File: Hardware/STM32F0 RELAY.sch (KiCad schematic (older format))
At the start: 28 parts, among them Q2 BSS138, U9 STM32F091RCT7, Y4 32.768kHz, Y5 8MHz

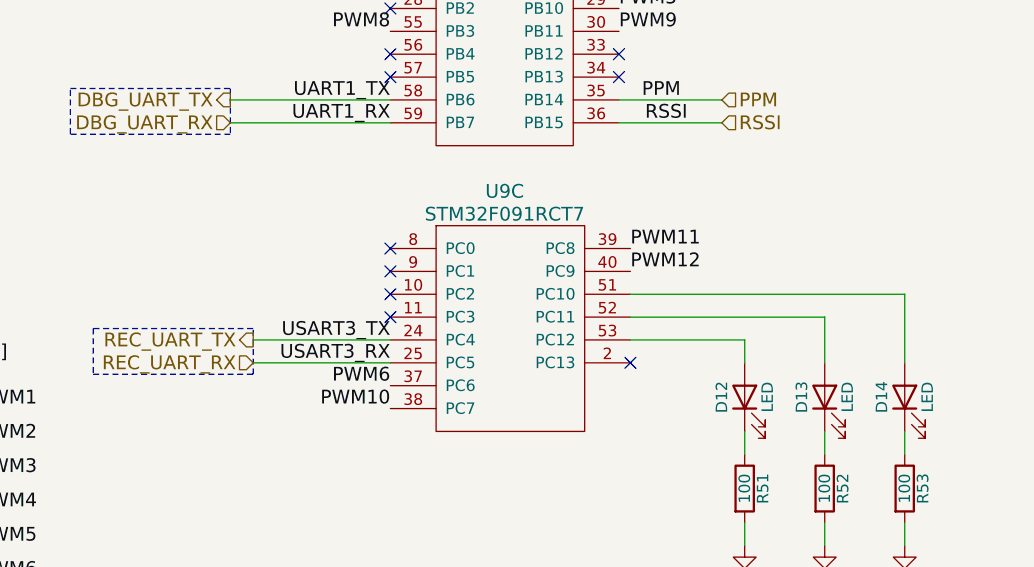
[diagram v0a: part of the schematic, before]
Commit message: Added additional headers to some interfaces, GPIOs, and FTDI pins. Added silks
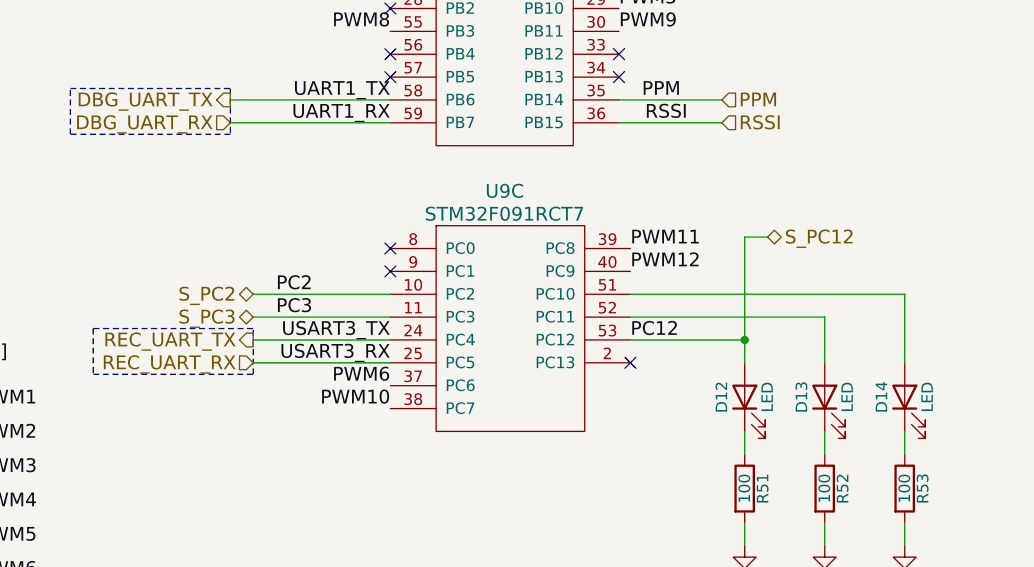
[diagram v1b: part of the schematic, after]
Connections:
- net S_PC12: now reaches D12.2 (A), U9.53 (PC12)
- net S_PC2: now reaches U9.10 (PC2)
- net S_PC3: now reaches U9.11 (PC3)
- no-connect marks 17 -> 15
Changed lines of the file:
@@
 $Descr A4 11693 8268
 encoding utf-8
-Sheet 9 10
+Sheet 8 10
 Title "Safety Switch Controller/ PPM Converter"
 Date "2017-05-14"
@@
 Wire Wire Line
 	7150 3150 7400 3150
-NoConn ~ 3900 5400
-NoConn ~ 3900 5300
 NoConn ~ 3900 5200
 NoConn ~ 3900 5100
@@
 Wire Wire Line
 	1400 2750 1400 2800
+Wire Wire Line
+	3900 5400 3300 5400
+Wire Wire Line
+	3900 5300 3300 5300
+Wire Wire Line
+	5450 5500 5450 5050
+Connection ~ 5450 5500
+Text Label 4950 5500 0    60   ~ 0
+PC12
+Text HLabel 3300 5300 0    60   BiDi ~ 0
+S_PC2
+Text HLabel 3300 5400 0    60   BiDi ~ 0
+S_PC3
+Text HLabel 5550 5050 2    60   BiDi ~ 0
+S_PC12
+Wire Wire Line
+	5450 5050 5550 5050
 Wire Bus Line
 	1850 5700 1850 7350
+Text Label 3400 5300 0    60   ~ 0
+PC2
+Text Label 3400 5400 0    60   ~ 0
+PC3
 $EndSCHEMATC

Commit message: associated components to their JLC part numbers
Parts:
- C65, C66: LCSC (none) -> C1644
- C67, C68: LCSC (none) -> C1679
- C69: LCSC (none) -> C57112
- C70: LCSC (none) -> C15849
- C71, C73, C74, C75: LCSC (none) -> C14663
- C72: LCSC (none) -> C19666
- D12, D13, D14: LCSC (none) -> C72043
- R5, R51, R52, R53, R6: LCSC (none) -> C22775
- R50: LCSC (none) -> C25803
- R54: LCSC (none) -> C25804
- U9: symbol WARG:STM32F091RCT7 -> ZP-Breakout-rescue:STM32F091RCT7-WARG; LCSC (none) -> C81046
- U9: symbol WARG:STM32F091RCT7 -> ZP-Breakout-rescue:STM32F091RCT7-WARG
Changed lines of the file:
@@
 EESchema Schematic File Version 4
-LIBS:ZP-Breakout-cache
-EELAYER 29 0
+EELAYER 30 0
 EELAYER END
 $Descr A4 11693 8268
@@
 F 3 "https://katalog.we-online.de/pbs/datasheet/885012006031.pdf" H 6550 2700 50  0001 C CNN
 F 4 "CAPP-009" H 6550 2700 60  0001 C CNN "part_num"
+F 5 "C1679" H 6550 2700 50  0001 C CNN "LCSC"
 	1    6550 2700
 	0    -1   -1   0
@@
 F 3 "https://katalog.we-online.de/pbs/datasheet/885012006031.pdf" H 6550 3000 50  0001 C CNN
 F 4 "CAPP-009" H 6550 3000 60  0001 C CNN "part_num"
+F 5 "C1679" H 6550 3000 50  0001 C CNN "LCSC"
 	1    6550 3000
 	0    -1   -1   0
@@
 F 3 "https://katalog.we-online.de/pbs/datasheet/885012006033.pdf" H 6550 2450 50  0001 C CNN
 F 4 "CAPP-008" H 6550 2450 60  0001 C CNN "part_num"
+F 5 "C1644" H 6550 2450 50  0001 C CNN "LCSC"
 	1    6550 2450
 	0    -1   -1   0
@@
 F 3 "https://katalog.we-online.de/pbs/datasheet/885012006033.pdf" H 6550 2150 50  0001 C CNN
 F 4 "CAPP-008" H 6550 2150 60  0001 C CNN "part_num"
+F 5 "C1644" H 6550 2150 50  0001 C CNN "LCSC"
 	1    6550 2150
 	0    -1   -1   0
@@
 F 3 "http://optoelectronics.liteon.com/upload/download/DS22-2000-228/LTST-C191KGKT.PDF" H 5800 5750 50  0001 C CNN
 F 4 "DIOD-002" H 5800 5750 60  0001 C CNN "part_num"
+F 5 "C72043" H 5800 5750 50  0001 C CNN "LCSC"
 	1    5800 5750
 	0    -1   -1   0
@@
 F 3 "http://www.yageo.com/documents/recent/PYu-RC_Group_51_RoHS_L_10.pdf" H 5800 6150 50  0001 C CNN
 F 4 "RESS-006" V 5800 6150 60  0001 C CNN "part_num"
+F 5 "C22775" V 5800 6150 50  0001 C CNN "LCSC"
 	1    5800 6150
 	1    0    0    -1
@@
 F 3 "http://optoelectronics.liteon.com/upload/download/DS22-2000-228/LTST-C191KGKT.PDF" H 5450 5750 50  0001 C CNN
 F 4 "DIOD-002" H 5450 5750 60  0001 C CNN "part_num"
+F 5 "C72043" H 5450 5750 50  0001 C CNN "LCSC"
 	1    5450 5750
 	0    -1   -1   0
@@
 F 3 "http://www.yageo.com/documents/recent/PYu-RC_Group_51_RoHS_L_10.pdf" H 5450 6150 50  0001 C CNN
 F 4 "RESS-006" V 5450 6150 60  0001 C CNN "part_num"
+F 5 "C22775" V 5450 6150 50  0001 C CNN "LCSC"
 	1    5450 6150
 	1    0    0    -1
@@
 F 3 "http://optoelectronics.liteon.com/upload/download/DS22-2000-228/LTST-C191KGKT.PDF" H 6150 5750 50  0001 C CNN
 F 4 "DIOD-002" H 6150 5750 60  0001 C CNN "part_num"
+F 5 "C72043" H 6150 5750 50  0001 C CNN "LCSC"
 	1    6150 5750
 	0    -1   -1   0
@@
 F 3 "http://www.yageo.com/documents/recent/PYu-RC_Group_51_RoHS_L_10.pdf" H 6150 6150 50  0001 C CNN
 F 4 "RESS-006" V 6150 6150 60  0001 C CNN "part_num"
+F 5 "C22775" V 6150 6150 50  0001 C CNN "LCSC"
 	1    6150 6150
 	1    0    0    -1
@@
 $EndComp
 $Comp
-L WARG:STM32F091RCT7 U9
+L ZP-Breakout-rescue:STM32F091RCT7-WARG U9
 U 5 1 599C1AE4
 P 8350 4900
@@
 F 3 "http://www.yageo.com/documents/recent/PYu-RC_Group_51_RoHS_L_10.pdf" H 7400 3300 50  0001 C CNN
 F 4 "RESS-005" V 7400 3300 60  0001 C CNN "part_num"
+F 5 " C25804" V 7400 3300 50  0001 C CNN "LCSC"
 	1    7400 3300
 	1    0    0    -1
@@
 F 3 "http://www.yageo.com/documents/recent/PYu-RC_Group_51_RoHS_L_10.pdf" H 2100 4350 50  0001 C CNN
 F 4 "RESS-008" V 2100 4350 60  0001 C CNN "part_num"
+F 5 "C25803" V 2100 4350 50  0001 C CNN "LCSC"
 	1    2100 4350
 	-1   0    0    -1
@@
 F 3 "https://search.murata.co.jp/Ceramy/image/img/A01X/G101/ENG/GRM188R71E104KA01-01.pdf" H 8400 5050 50  0001 C CNN
 F 4 "CAPP-005" H 8400 5050 60  0001 C CNN "part_num"
+F 5 "C14663" H 8400 5050 50  0001 C CNN "LCSC"
 	1    8400 5050
 	1    0    0    -1
@@
 F 3 "https://search.murata.co.jp/Ceramy/image/img/A01X/G101/ENG/GRM188R71H103KA01-01.pdf" H 6900 5050 50  0001 C CNN
 F 4 "CAPP-010" H 6900 5050 60  0001 C CNN "part_num"
+F 5 "C57112" H 6900 5050 50  0001 C CNN "LCSC"
 	1    6900 5050
 	1    0    0    -1
@@
 F 3 "https://search.murata.co.jp/Ceramy/image/img/A01X/G101/ENG/GRM188R61E105KA12-01.pdf" H 7150 5050 50  0001 C CNN
 F 4 "CAPP-004" H 7150 5050 60  0001 C CNN "part_num"
+F 5 "C15849" H 7150 5050 50  0001 C CNN "LCSC"
 	1    7150 5050
 	1    0    0    -1
@@
 F 3 "http://www.samsungsem.com/kr/support/product-search/mlcc/CL10A475MP5LNNC.jsp" H 7650 5050 50  0001 C CNN
 F 4 "CAPP-006" H 7650 5050 60  0001 C CNN "part_num"
+F 5 "C19666" H 7650 5050 50  0001 C CNN "LCSC"
 	1    7650 5050
 	1    0    0    -1
@@
 F 3 "https://search.murata.co.jp/Ceramy/image/img/A01X/G101/ENG/GRM188R71E104KA01-01.pdf" H 8150 5050 50  0001 C CNN
 F 4 "CAPP-005" H 8150 5050 60  0001 C CNN "part_num"
+F 5 "C14663" H 8150 5050 50  0001 C CNN "LCSC"
 	1    8150 5050
 	1    0    0    -1
@@
 F 3 "https://search.murata.co.jp/Ceramy/image/img/A01X/G101/ENG/GRM188R71E104KA01-01.pdf" H 7900 5050 50  0001 C CNN
 F 4 "CAPP-005" H 7900 5050 60  0001 C CNN "part_num"
+F 5 "C14663" H 7900 5050 50  0001 C CNN "LCSC"
 	1    7900 5050
 	1    0    0    -1
@@
 F 3 "https://search.murata.co.jp/Ceramy/image/img/A01X/G101/ENG/GRM188R71E104KA01-01.pdf" H 7400 5050 50  0001 C CNN
 F 4 "CAPP-005" H 7400 5050 60  0001 C CNN "part_num"
+F 5 "C14663" H 7400 5050 50  0001 C CNN "LCSC"
 	1    7400 5050
 	1    0    0    -1
@@
 NoConn ~ 3950 2750
 $Comp
-L WARG:STM32F091RCT7 U9
+L ZP-Breakout-rescue:STM32F091RCT7-WARG U9
 U 1 1 599C1943
 P 4400 3200
@@
 F 3 "http://www.st.com/content/ccc/resource/technical/document/datasheet/95/3c/2e/5b/21/09/45/a6/DM00115237.pdf/files/DM00115237.pdf/jcr:content/translations/en.DM00115237.pdf" H 4150 3700 60  0001 C CNN
 F 4 "CHIP-008" H 4500 4300 60  0001 C CNN "part_num"
+F 5 "C81046" H 4400 3200 50  0001 C CNN "LCSC"
 	1    4400 3200
 	1    0    0    -1
 $EndComp
 $Comp
-L WARG:STM32F091RCT7 U9
+L ZP-Breakout-rescue:STM32F091RCT7-WARG U9
 U 3 1 599C1A21
 P 4400 5850
@@
 $EndComp
 $Comp
-L WARG:STM32F091RCT7 U9
+L ZP-Breakout-rescue:STM32F091RCT7-WARG U9
 U 2 1 599C19BB
 P 4400 4600
@@
 $EndComp
 $Comp
-L WARG:STM32F091RCT7 U9
+L ZP-Breakout-rescue:STM32F091RCT7-WARG U9
 U 4 1 599C1A7B
 P 8000 3000
@@
 F 3 "http://www.yageo.com/documents/recent/PYu-RC_Group_51_RoHS_L_10.pdf" H 1400 3250 50  0001 C CNN
 F 4 "RESS-006" V 1400 3250 60  0001 C CNN "part_num"
+F 5 "C22775" V 1400 3250 50  0001 C CNN "LCSC"
 	1    1400 3250
 	1    0    0    -1
@@
 F 3 "http://www.yageo.com/documents/recent/PYu-RC_Group_51_RoHS_L_10.pdf" H 1400 2950 50  0001 C CNN
 F 4 "RESS-006" V 1400 2950 60  0001 C CNN "part_num"
+F 5 "C22775" V 1400 2950 50  0001 C CNN "LCSC"
 	1    1400 2950
 	1    0    0    -1
